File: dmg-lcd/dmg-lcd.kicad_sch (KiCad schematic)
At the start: 2 parts, among them J1 Conn_01x01_Pin, J2 Conn_01x01_Pin

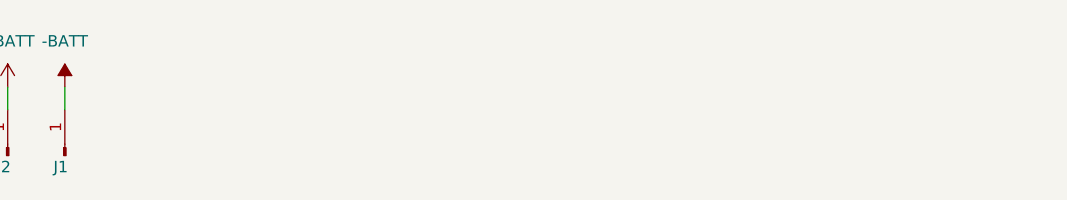
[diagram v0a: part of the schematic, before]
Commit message: feat: Add potentiometers and volumn switch
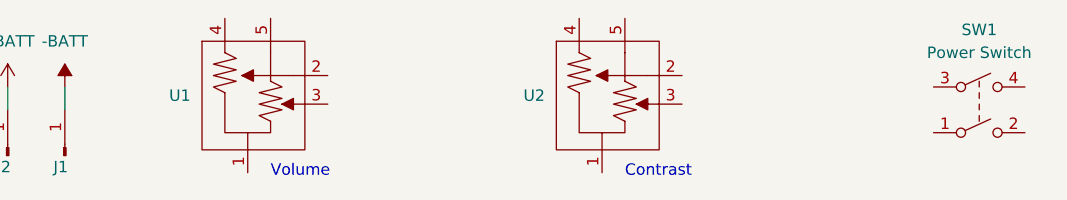
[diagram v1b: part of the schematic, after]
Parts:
- added SW1: Power Switch, dmg-lcd:Power_Switch, symbol Switch:SW_DPST
- added U1: ~, dmg-lcd:Volume_Potentiometer, symbol DMG_LCD:Dual_Potentiometer
- added U2: ~, dmg-lcd:Contrast_Potentiometer, symbol DMG_LCD:Dual_Potentiometer
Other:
- note added: "Contrast"
- note added: "Volume"
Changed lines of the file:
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@@
     (stroke (width 0) (type default))
+  )
+  (text "Contrast" (at 153.67 153.67 0)
+    (effects (font (size 1.27 1.27)) (justify left bottom))
+  )
+  (text "Volume" (at 114.3 153.67 0)
+    (effects (font (size 1.27 1.27)) (justify left bottom))
+  )
+  (symbol (lib_id "DMG_LCD:Dual_Potentiometer") (at 111.76 143.51 0) (unit 1)
+    (in_bom yes) (on_board yes) (dnp no) (fields_autoplaced)
+    (property "Reference" "U1" (at 105.41 144.4625 0)
+      (effects (font (size 1.27 1.27)) (justify right))
+    )
+    (property "Value" "~" (at 121.92 152.4 0)
+      (effects (font (size 1.27 1.27)))
+    )
+    (property "Footprint" "dmg-lcd:Volume_Potentiometer" (at 121.92 152.4 0)
+      (effects (font (size 1.27 1.27)) hide)
+    )
+    (property "Datasheet" "" (at 121.92 152.4 0)
+      (effects (font (size 1.27 1.27)) hide)
+    )
+    (pin "1")
+    (pin "2")
+    (pin "3")
+    (pin "4")
+    (pin "5")
+    (instances
+      (project "dmg-lcd"
+        (path "/3c151911-a223-4c8f-9e4a-ec69f6a11d36"
+          (reference "U1") (unit 1)
+        )
+      )
+    )
   )
   (symbol (lib_id "Connector:Conn_01x01_Pin") (at 85.09 151.13 90) (unit 1)
@@
     )
   )
+  (symbol (lib_id "Switch:SW_DPST") (at 193.04 146.05 0) (unit 1)
+    (in_bom yes) (on_board yes) (dnp no) (fields_autoplaced)
+    (property "Reference" "SW1" (at 193.04 137.16 0)
+      (effects (font (size 1.27 1.27)))
+    )
+    (property "Value" "Power Switch" (at 193.04 139.7 0)
+      (effects (font (size 1.27 1.27)))
+    )
+    (property "Footprint" "dmg-lcd:Power_Switch" (at 193.04 146.05 0)
+      (effects (font (size 1.27 1.27)) hide)
+    )
+    (property "Datasheet" "~" (at 193.04 146.05 0)
+      (effects (font (size 1.27 1.27)) hide)
+    )
+    (pin "1")
+    (pin "2")
+    (pin "3")
+    (pin "4")
+    (instances
+      (project "dmg-lcd"
+        (path "/3c151911-a223-4c8f-9e4a-ec69f6a11d36"
+          (reference "SW1") (unit 1)
+        )
+      )
+    )
+  )
   (symbol (lib_id "power:-BATT") (at 91.44 143.51 0) (unit 1)
     (in_bom yes) (on_board yes) (dnp no) (fields_autoplaced)
@@
         )
       )
+    )
+  )
+  (symbol (lib_id "DMG_LCD:Dual_Potentiometer") (at 151.13 143.51 0) (unit 1)
+    (in_bom yes) (on_board yes) (dnp no) (fields_autoplaced)
+    (property "Reference" "U2" (at 144.78 144.4625 0)
+      (effects (font (size 1.27 1.27)) (justify right))
+    )
+    (property "Value" "~" (at 161.29 152.4 0)
+      (effects (font (size 1.27 1.27)))
+    )
+    (property "Footprint" "dmg-lcd:Contrast_Potentiometer" (at 161.29 152.4 0)
+      (effects (font (size 1.27 1.27)) hide)
+    )
+    (property "Datasheet" "" (at 161.29 152.4 0)
+      (effects (font (size 1.27 1.27)) hide)
+    )
+    (pin "1")
+    (pin "2")
+    (pin "3")
+    (pin "4")
+    (pin "5")
+    (instances
+      (project "dmg-lcd"
+        (path "/3c151911-a223-4c8f-9e4a-ec69f6a11d36"
+          (reference "U2") (unit 1)
+        )
+      )

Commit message: feat: V1.0 of the board
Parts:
- added C1: 330nF, Capacitor_SMD:C_0603_1608Metric, symbol Device:C
- added C2: 200nF, Capacitor_SMD:C_0603_1608Metric, symbol Device:C
- added C3, C4: 2.2uF, Capacitor_SMD:C_0603_1608Metric, symbol Device:C
- added J10: Conn_01x01, Connector_PinHeader_2.54mm:PinHeader_1x01_P2.54mm_Vertical, symbol Connector_Generic:Conn_01x01
- added J3: LCD Connector, Connector_FFC-FPC:TE_3-1734839-0_1x30-1MP_P0.5mm_Horizontal, symbol Connector_Generic:Conn_01x30
- added J4: LCD Dev Header, Connector_PinHeader_2.54mm:PinHeader_1x15_P2.54mm_Vertical, symbol Connector_Generic:Conn_01x15
- added J5, J8, J9: Conn_01x02, Connector_PinHeader_2.54mm:PinHeader_1x02_P2.54mm_Vertical, symbol Connector_Generic:Conn_01x02
- added J6, J7: Conn_01x05, Connector_PinHeader_2.54mm:PinHeader_1x05_P2.54mm_Vertical, symbol Connector_Generic:Conn_01x05
- added R1: 10M, Resistor_SMD:R_0603_1608Metric, symbol Device:R_US
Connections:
- net +BATT: now also J10.1 (Pin_1)
- net at U1.1: now also J6.5 (Pin_5)
- net at U1.2: now also J6.3 (Pin_3)
- net at U1.3: now also J6.4 (Pin_4)
- net at U1.4: now also J6.1 (Pin_1)
- net at U1.5: now also J6.2 (Pin_2)
- net at SW1.1: now also J9.2 (Pin_2)
- net at SW1.2: now also J9.1 (Pin_1)
- net at SW1.3: now also J8.1 (Pin_1)
- net at SW1.4: now also J8.2 (Pin_2)
- net at U2.1: now also J7.5 (Pin_5)
- net at U2.2: now also J7.3 (Pin_3)
- net at U2.3: now also J7.4 (Pin_4)
- net at U2.4: now also J7.1 (Pin_1)
- net at U2.5: now also J7.2 (Pin_2)
- net -BATT renamed GND
- net GND: now also C1.2, J3.13 (Pin_13), J5.2 (Pin_2), R1.2
- new net +3.3V: J3.11 (Pin_11), J3.12 (Pin_12), J5.1 (Pin_1)
- new net BM0: J3.15 (Pin_15), J4.2 (Pin_2)
- new net BM1: J3.14 (Pin_14), J4.1 (Pin_1)
- new net CD: J3.17 (Pin_17), J4.4 (Pin_4)
- new net CS0: J3.16 (Pin_16), J4.3 (Pin_3)
- new net D0: J3.21 (Pin_21), J4.8 (Pin_8)
- new net D1: J3.22 (Pin_22), J4.9 (Pin_9)
- new net D2: J3.23 (Pin_23), J4.10 (Pin_10)
- new net D3: J3.24 (Pin_24), J4.11 (Pin_11)
- new net D4: J3.25 (Pin_25), J4.12 (Pin_12)
- new net D5: J3.26 (Pin_26), J4.13 (Pin_13)
- new net D6: J3.27 (Pin_27), J4.14 (Pin_14)
- new net D7: J3.28 (Pin_28), J4.15 (Pin_15)
- new net RD(E): J3.18 (Pin_18), J4.5 (Pin_5)
- new net RST: J3.20 (Pin_20), J4.7 (Pin_7)
- new net VB0+: C3.1, J3.10 (Pin_10)
- new net VB0-: C3.2, J3.7 (Pin_7)
- new net VB1+: C4.1, J3.9 (Pin_9)
- new net VB1-: C4.2, J3.8 (Pin_8)
- new net VLCD_In: C1.1, J3.3 (Pin_3), J3.4 (Pin_4), R1.1
- new net VS+: C2.1, J3.5 (Pin_5)
- new net VS-: C2.2, J3.6 (Pin_6)
- new net WR: J3.19 (Pin_19), J4.6 (Pin_6)
- no-connect marks 0 -> 4

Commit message: feat: Update one of the capacitor footprints to match what is in stock, rerouting too
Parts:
- C2: footprint Capacitor_SMD:C_0603_1608Metric -> Capacitor_SMD:C_1206_3216Metric
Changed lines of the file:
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@@
       (effects (font (size 1.27 1.27)) (justify left))
     )
-    (property "Footprint" "Capacitor_SMD:C_0603_1608Metric" (at 187.6552 100.33 0)
+    (property "Footprint" "Capacitor_SMD:C_1206_3216Metric" (at 187.6552 100.33 0)
       (effects (font (size 1.27 1.27)) hide)
     )
